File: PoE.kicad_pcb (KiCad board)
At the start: 4 copper layers, 102.5 x 35 mm, 109 parts, among them J1 Conn_01x03, J1001 8P8C_LED_Shielded_x2, J1002 8P8C_LED_Shielded_x2, Q2 MMBT3906, Q2001 SI7898DP-T1-E3, U1 TPS563203, U1001 7490220122, U1002 TCMT1107, U2001 TPS23751PWP, U2002 TCMT1107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

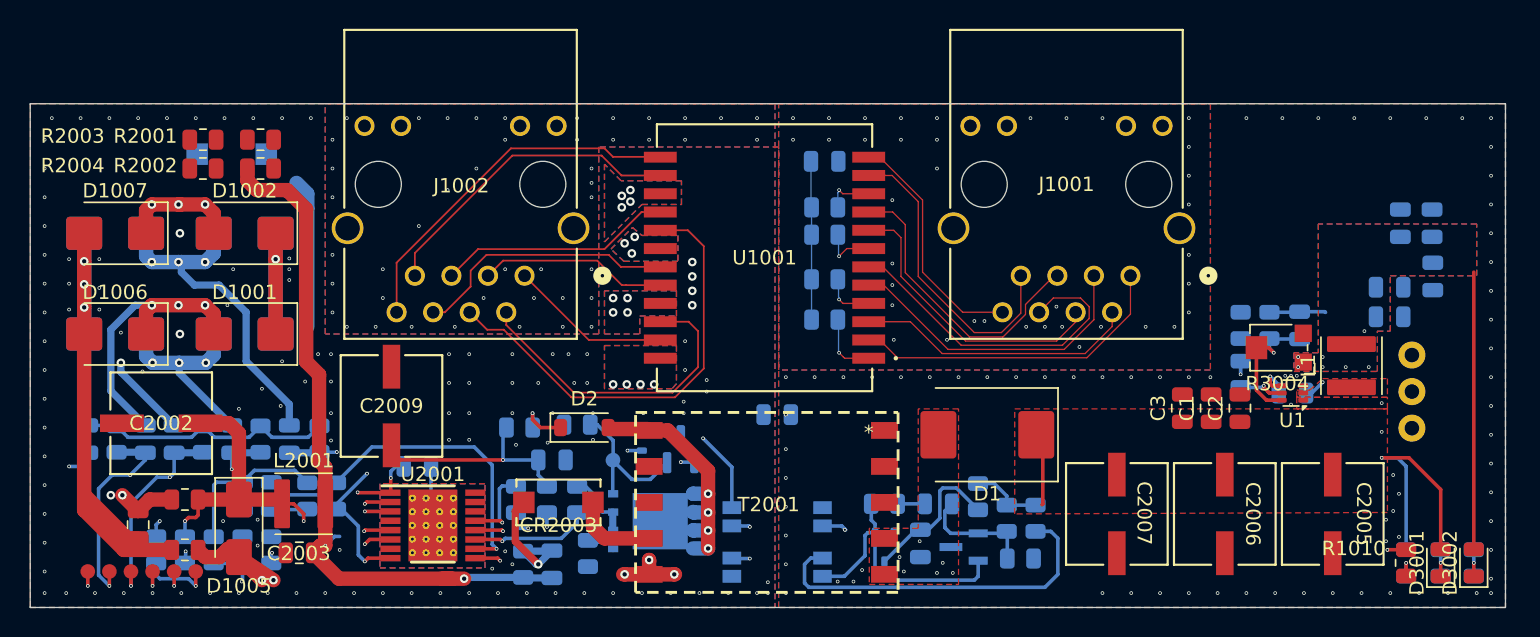
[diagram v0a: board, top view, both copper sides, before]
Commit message: Updated layout and constraints
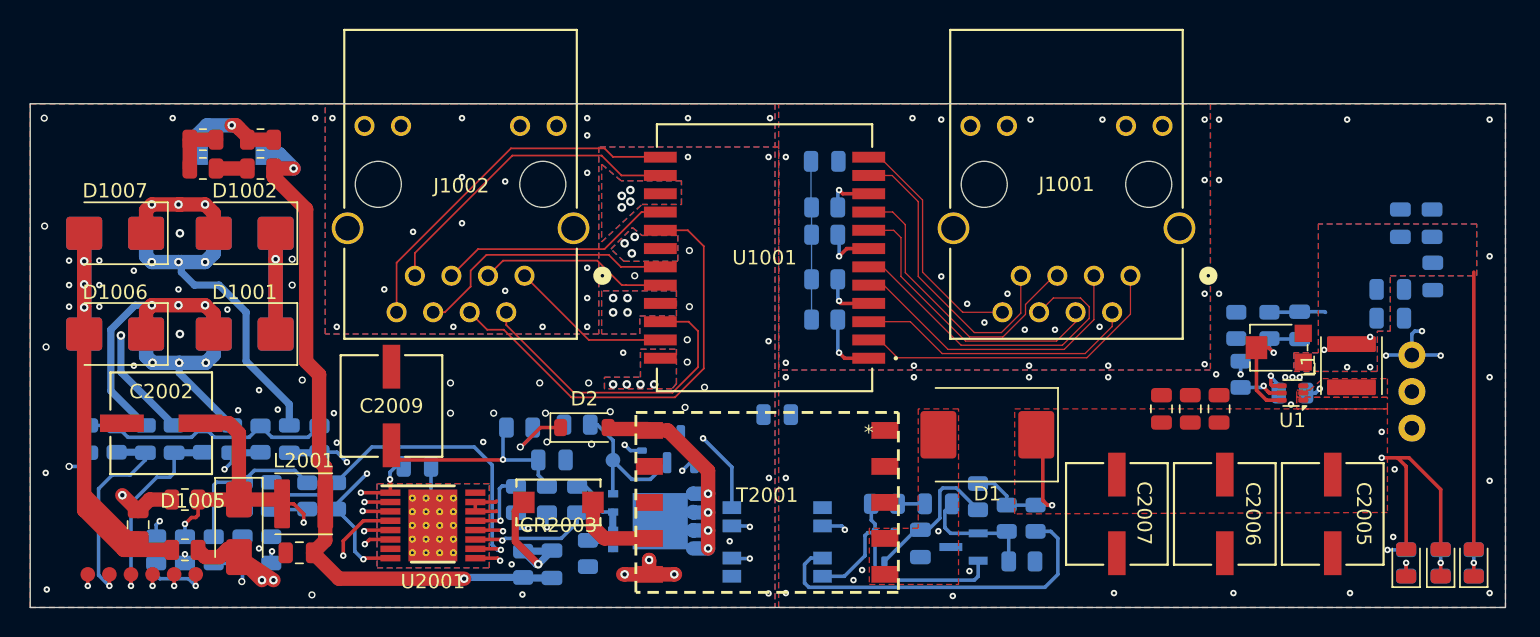
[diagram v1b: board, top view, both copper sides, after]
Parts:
- D1010: moved to F.Cu
- R1010: moved to B.Cu
- moved C1 1.45 mm to (123.1, 44.2)
- moved C2 1.45 mm to (125.1, 44.2)
- moved C3 1.45 mm to (121.1, 44.2)
- moved R2 0.30 mm to (126.3, 38.4)
- moved R2021 0.22 mm to (111.4, 54.8)
- moved TP1001 0.20 mm to (46.5, 55.7)
- moved TP1002 0.20 mm to (52.5, 55.7)
- moved TP1003 0.20 mm to (51.0, 55.7)
- moved TP1004 0.20 mm to (49.5, 55.7)
- moved TP1005 0.20 mm to (48.0, 55.7)
- moved TP1006 0.20 mm to (54.0, 55.7)
- moved C6 0.16 mm to (137.0, 35.9)
- moved C7 0.11 mm to (137.0, 37.9)
- turned R2002 to 180 degrees
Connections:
- net /Flyback/5V_PRI renamed /Flyback/12V_PRI
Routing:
- net /Flyback/T_PRI: track 85.7 -> 73.3 mm
- net GND: track 0.00 -> 8.52 mm, vias 119 -> 56
- net Net-(CR2001-Pad2): track 0.00 -> 7.45 mm, vias 0 -> 1
- net GNDREF: track 0.00 -> 6.08 mm, vias 81 -> 33
- net Net-(R2003-Pad1): track 0.00 -> 3.83 mm
- net APD: track 0.00 -> 2.17 mm
- net Net-(D2-K): track 3.63 -> 5.25 mm
- net Net-(D3-A): track 16.9 -> 18.1 mm
- net Net-(U2001-CTL): track 75.9 -> 74.8 mm
- net Net-(U2001-CLS): track 18.3 -> 17.5 mm
- net /VDD_PRIME: track 40.2 -> 39.4 mm, vias 3 -> 2
- net Net-(U2001-VB): track 32.7 -> 33.3 mm
- net /TEST_C: track 25.9 -> 26.5 mm
- net +12V: track 32.1 -> 32.6 mm
- net Net-(U2001-DEN): track 17.3 -> 17.0 mm, vias 1 -> 2
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
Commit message: Minor changes
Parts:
- C10, C6, C7, C8, C9: moved to F.Cu
- moved C9 8.77 mm to (131.9, 34.9), turned to 180 degrees
- moved C10 8.06 mm to (131.9, 36.9), turned to 180 degrees
- moved C6 2.00 mm to (137.0, 37.9)
- moved C7 2.00 mm to (137.0, 35.9)
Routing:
- net Net-(J1-Pin_2): track 13.6 -> 17.9 mm
- net VOUT1: track 23.2 -> 24.5 mm
- net Net-(U2001-VB): track 33.3 -> 34.0 mm
- net GNDREF: vias 33 -> 38
- net GND: vias 56 -> 58
- removed copper zone on B.Cu, net VOUT1
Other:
- board text added: "12V"
- board text added: "5V"
- board text added: "APD"

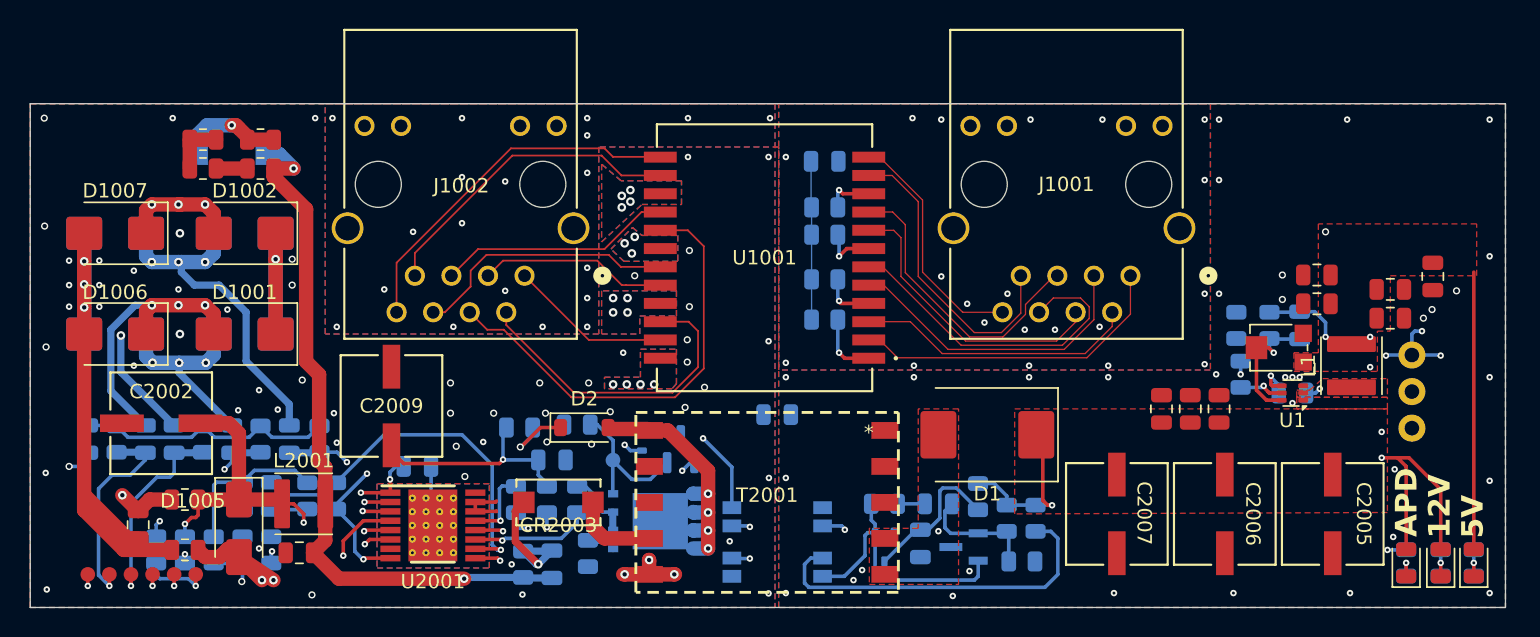
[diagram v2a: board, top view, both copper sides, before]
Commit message: Redoing ethernet routing
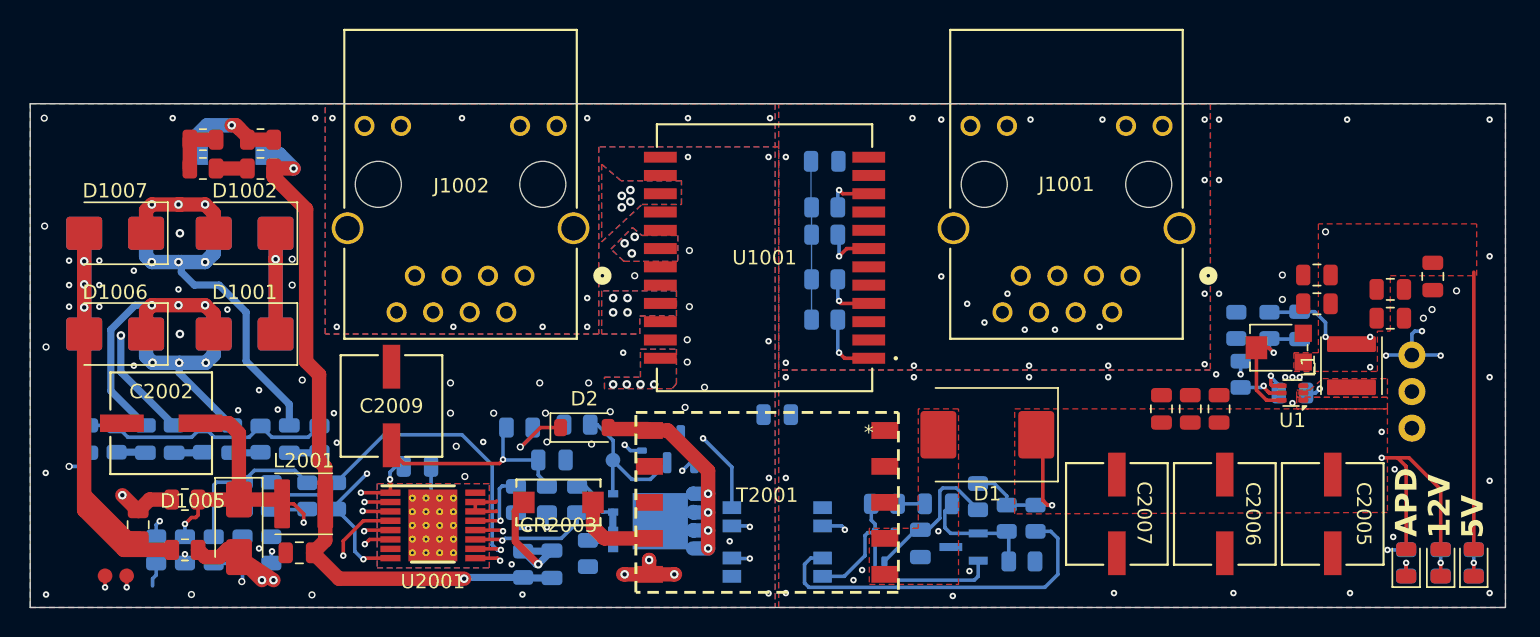
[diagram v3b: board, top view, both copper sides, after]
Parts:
- removed TP1002, TP1003, TP1004, TP1005: TestPoint, SparkFun-Connector:TestPoint-1.0mm
- R2009: value 63..4k -> 63.4k
- moved TP1006 4.80 mm to (49.2, 55.8)
- moved TP1001 1.20 mm to (47.7, 55.8)
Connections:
- net /TEST_A renamed Net-(C1002-Pad2)
- net /TEST_B renamed Net-(C1003-Pad2)
- net /TEST_C renamed Net-(C1004-Pad2)
- net /TEST_D renamed Net-(C1005-Pad2)
- J1002 pad 4: /POE1_N -> /POE2_N
- J1002 pad 6: /POE2_N -> /POE1_N
- U1001 pad 16: /POE2_P -> /POE2_N
- U1001 pad 17: /POE1_N -> /POE2_P
- U1001 pad 19: /POE2_N -> /POE1_N
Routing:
- net /POE1_N: track 31.5 -> 0.00 mm
- net /POE3_N: track 25.3 -> 0.04 mm
- net Net-(C1004-Pad2): track 26.5 -> 2.12 mm, vias 2 -> 0
- net /ETH3: track 23.3 -> 0.97 mm
- net /POE0_N: track 22.3 -> 0.00 mm
- net /POE3_P: track 22.0 -> 0.00 mm
- net /ETH0: track 22.6 -> 0.76 mm
- net /ETH6: track 21.3 -> 0.00 mm
- net /ETH5: track 20.8 -> 0.21 mm
- net /ETH2: track 21.4 -> 1.04 mm
- net /ETH4: track 20.4 -> 0.67 mm
- net /ETH1: track 20.6 -> 1.04 mm
- net /POE2_N: track 18.4 -> 0.00 mm
- net /POE2_P: track 16.3 -> 0.00 mm
- net /ETH7: track 16.7 -> 0.76 mm
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
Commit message: Fixing ethernet routing
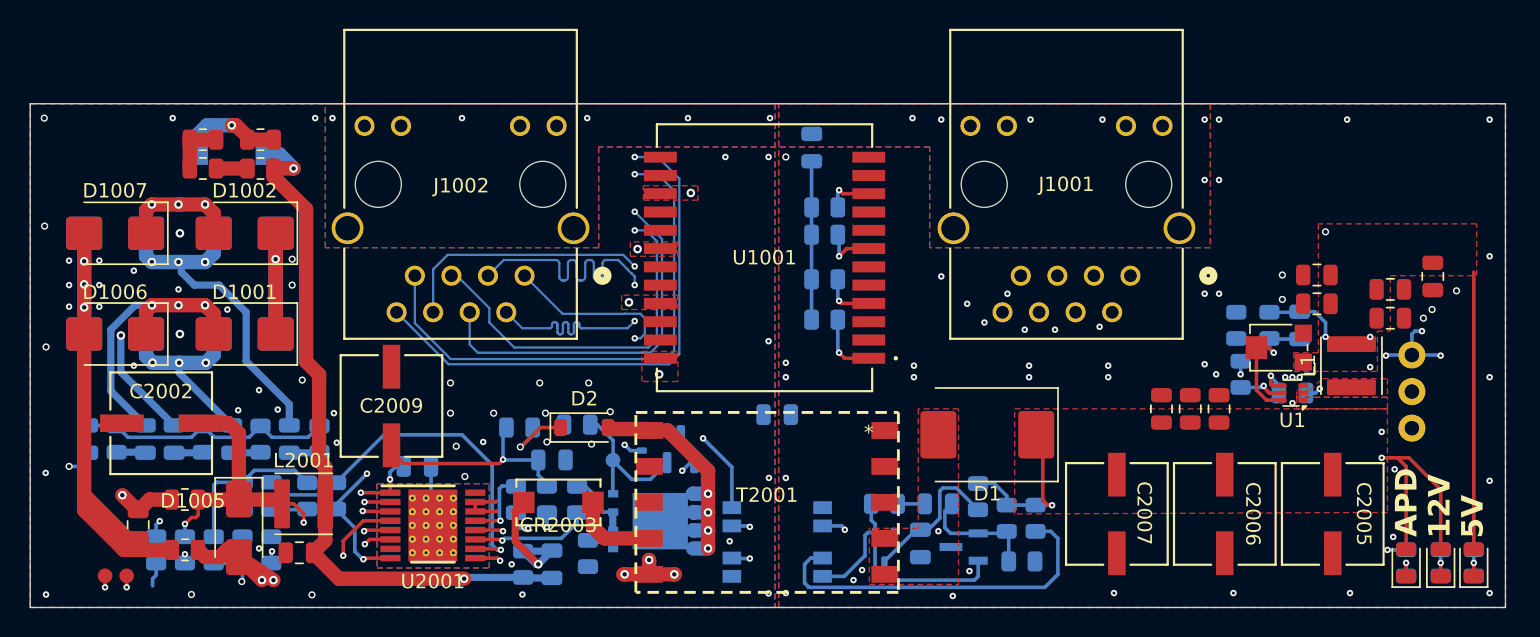
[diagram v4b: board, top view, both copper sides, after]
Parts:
- moved C1001 1.31 mm to (96.8, 26.1), turned to 90 degrees
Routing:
- net /POE3_N: track 0.04 -> 37.4 mm, vias 0 -> 1
- net /POE3_P: track 0.00 -> 36.9 mm, vias 0 -> 1
- net /POE2_N: track 0.00 -> 26.0 mm, vias 0 -> 1
- net /POE2_P: track 0.00 -> 25.8 mm, vias 0 -> 1
- net /POE1_P: track 0.00 -> 18.9 mm, vias 0 -> 1
- net /POE1_N: track 0.00 -> 17.7 mm, vias 0 -> 1
- net /POE0_N: track 0.00 -> 12.9 mm, vias 0 -> 1
- net /POE0_P: track 0.17 -> 11.7 mm, vias 0 -> 1
- net /D_IN: track 75.8 -> 71.9 mm, vias 7 -> 4
- net /A_IN: track 54.5 -> 57.9 mm, vias 7 -> 4
- net /C_IN: track 71.8 -> 71.3 mm, vias 6 -> 4
- net /B_IN: track 66.4 -> 66.2 mm, vias 8 -> 5
- net GNDREF: vias 38 -> 39
- net GNDPWR: vias 31 -> 25
- net GND: vias 59 -> 51
- removed copper zone on B.Cu, net /A_IN
- removed copper zone on In1.Cu, net /A_IN
- removed copper zone on In2.Cu, net /A_IN
- removed copper zone on B.Cu, net /B_IN
- removed copper zone on In1.Cu, net /B_IN
- removed copper zone on In2.Cu, net /B_IN
- removed copper zone on B.Cu, net /C_IN
- removed copper zone on In1.Cu, net /C_IN
- removed copper zone on In2.Cu, net /C_IN
- removed copper zone on B.Cu, net /D_IN
- removed copper zone on In1.Cu, net /D_IN
- removed copper zone on In2.Cu, net /D_IN

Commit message: Routing updates to ethernet
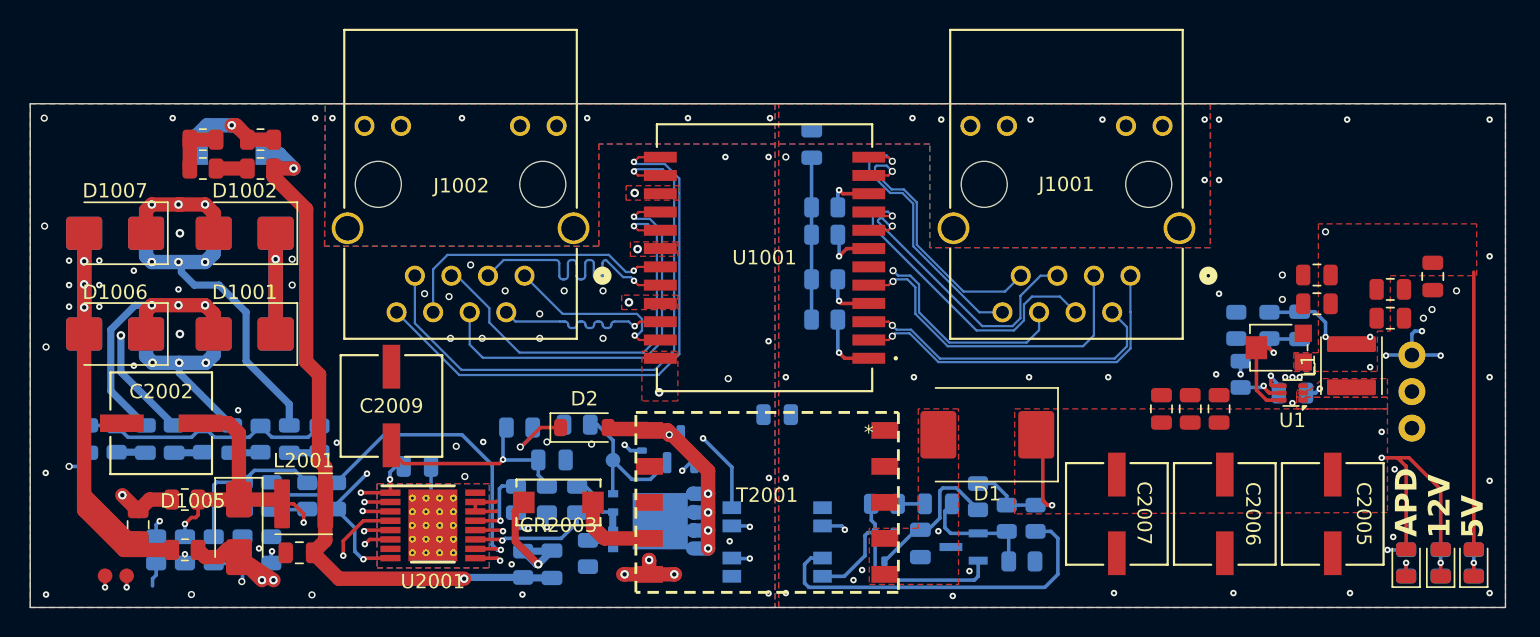
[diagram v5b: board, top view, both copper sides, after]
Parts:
- moved C1001 0.25 mm to (96.8, 25.8)
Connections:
- net /ETH0 renamed /ETH0_P
- net /ETH1 renamed /ETH0_N
- net /ETH2 renamed /ETH1_P
- net /ETH3 renamed /ETH1_N
- net /ETH6 renamed /ETH3_P
- net /ETH7 renamed /ETH3_N
- J1001 pad 4: /ETH4 -> /ETH2_N
- J1001 pad 5: /ETH5 -> /ETH2_P
- U1001 pad 8: /ETH4 -> /ETH2_P
- U1001 pad 9: /ETH5 -> /ETH2_N
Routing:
- net /ETH0_P: track 0.76 -> 25.4 mm, vias 0 -> 1
- net /ETH2_N: track 0.00 -> 24.0 mm, vias 0 -> 1
- net /ETH1_P: track 1.04 -> 24.4 mm, vias 0 -> 1
- net /ETH0_N: track 1.04 -> 23.2 mm, vias 0 -> 1
- net /ETH2_P: track 0.00 -> 21.2 mm, vias 0 -> 1
- net /ETH3_P: track 0.00 -> 19.3 mm, vias 0 -> 1
- net /ETH3_N: track 0.76 -> 19.7 mm, vias 0 -> 1
- net /ETH1_N: track 0.97 -> 16.0 mm, vias 0 -> 1
- net GNDPWR: track 31.7 -> 39.8 mm, vias 25 -> 12
- net /B_IN: track 66.2 -> 70.3 mm
- net /POE3_P: track 36.9 -> 40.2 mm
- net /POE2_P: track 25.8 -> 28.7 mm
- net /POE3_N: track 37.4 -> 39.9 mm
- net /POE2_N: track 26.0 -> 28.4 mm
- net /POE1_N: track 17.7 -> 19.8 mm
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
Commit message: Routing updates to ethernet
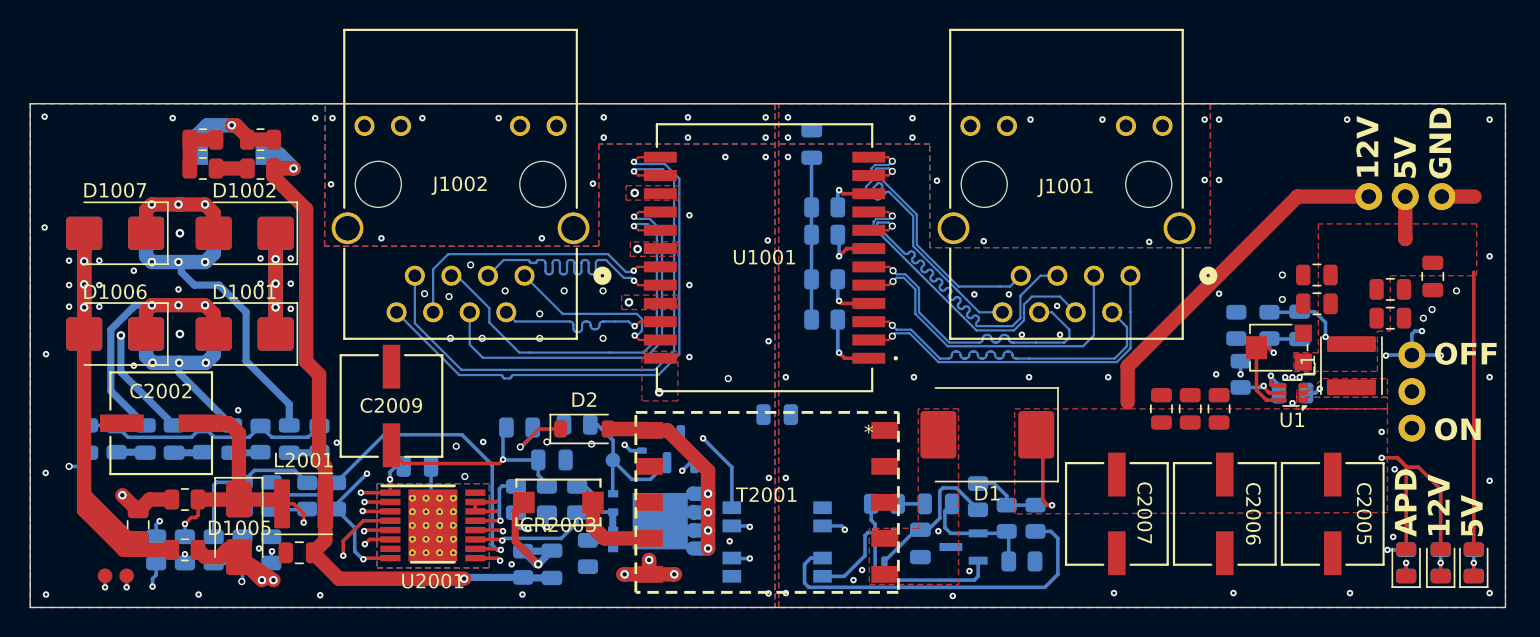
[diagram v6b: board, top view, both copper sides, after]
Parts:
- added J3001: Conn_01x03, SparkFun-Connector:1x03, F.Cu at (140.6, 29.4)
- moved D2 0.10 mm to (81.0, 45.6)
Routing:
- net +12V: track 32.6 -> 56.7 mm
- net /ETH1_N: track 16.0 -> 22.6 mm
- net /ETH2_P: track 21.2 -> 26.4 mm
- net VOUT1: track 24.5 -> 27.4 mm, vias 4 -> 1
- net GNDREF: track 6.08 -> 8.35 mm, vias 39 -> 44
- net /ETH0_N: track 23.2 -> 25.3 mm
- net /ETH3_N: track 19.7 -> 21.6 mm
- net /ETH3_P: track 19.3 -> 18.2 mm
- net /C_IN: track 72.0 -> 73.0 mm
- net /ETH2_N: track 24.0 -> 23.4 mm
- net Net-(D2-A): track 17.7 -> 17.5 mm, vias 5 -> 4
- net VSS: vias 3 -> 4
- net GNDPWR: vias 12 -> 25
- net GND: vias 51 -> 58
- net /VDD_PRIME: vias 2 -> 4
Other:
- board text added: "GND"
- board text added: "OFF"
- board text added: "ON"

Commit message: Updated clearence of GND and moved stitching vias around
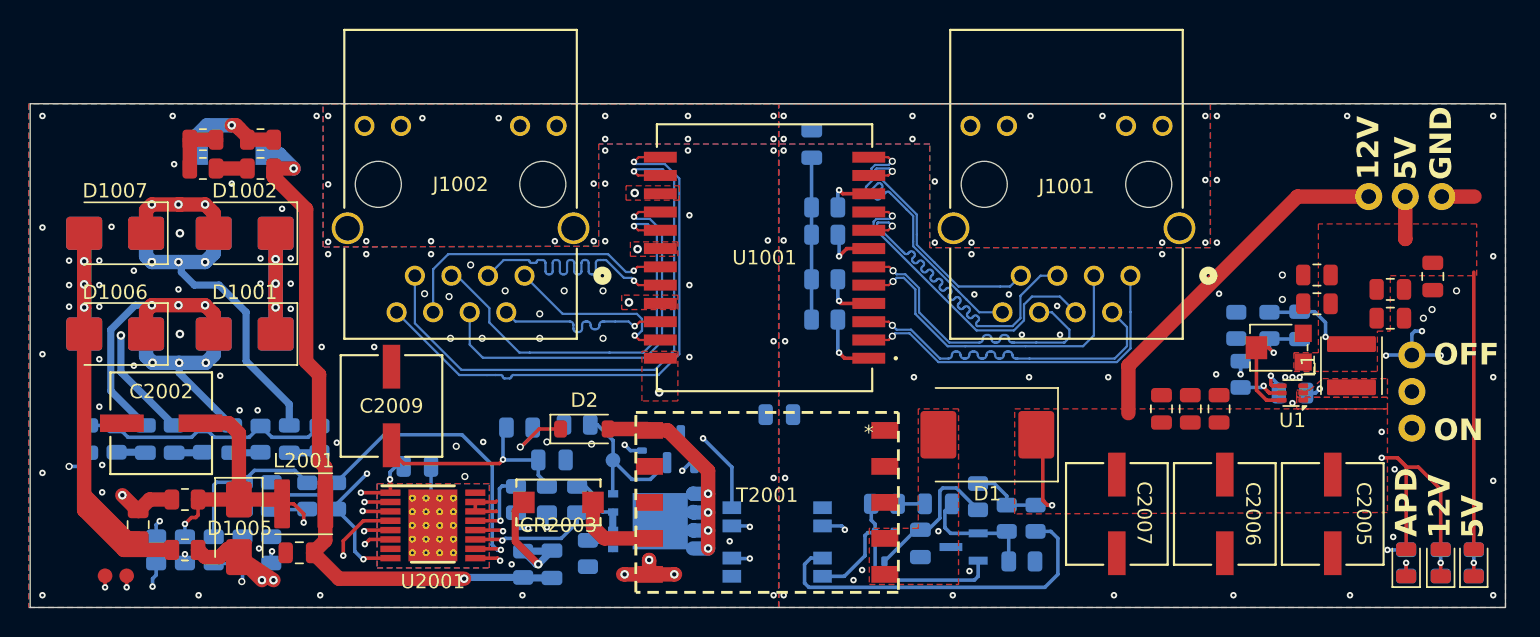
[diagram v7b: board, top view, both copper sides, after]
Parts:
- moved C2001 0.15 mm to (94.5, 44.6)
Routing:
- net +12V: track 56.7 -> 57.5 mm
- net GNDPWR: vias 25 -> 30
- net GNDREF: vias 44 -> 48
- net GND: vias 58 -> 75
